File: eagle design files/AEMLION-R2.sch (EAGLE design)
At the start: 17 parts, among them IC1 AEM10941, Q1 DMG1012UW, Q2 DMP2160UW

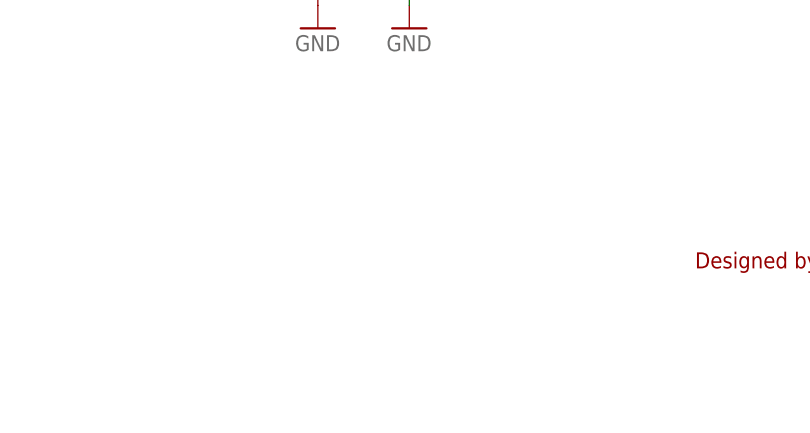
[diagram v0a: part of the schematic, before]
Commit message: Revision 2B Reduced the paste under IC1 to 50% of the exposed pad
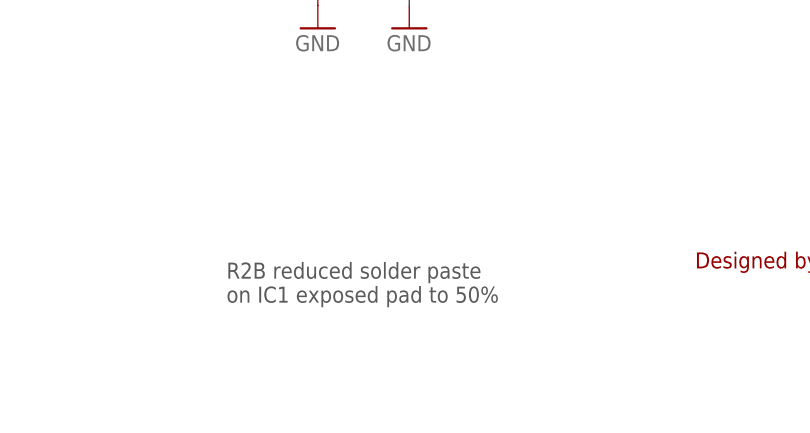
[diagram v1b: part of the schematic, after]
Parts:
- IC1: device sodaq:AEM10941 -> TSEM:AEM10941
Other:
- note added: "R2B reduced solder paste on IC1 exposed pad to 50%"
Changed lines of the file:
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@@
 </classes>
 <parts>
-<part name="IC1" library="sodaq" deviceset="AEM10941" device="" package3d_urn="urn:adsk.eagle:package:2265650/1" value="AEM10941"/>
+<part name="IC1" library="TSEM" deviceset="AEM10941" device="" value="AEM10941"/>
 <part name="GND6" library="supply1" deviceset="GND" device=""/>
 <part name="L2" library="TSEM" deviceset="L" device="0603_10UH" value="10uH"/>
@@
 voltage
 protection</text>
+<text x="163.83" y="16.51" size="1.778" layer="97">R2B reduced solder paste
+on IC1 exposed pad to 50%</text>
 </plain>
 <instances>
@@
 will not be understood (or retained) with this version.
 </note>
-<note version="8.3" severity="warning">
-Since Version 8.3, EAGLE supports the association of 3D packages
-with devices in libraries, schematics, and board files. Those 3D
-packages will not be understood (or retained) with this version.
-</note>
 </compatibility>
